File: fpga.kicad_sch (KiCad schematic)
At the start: 36 parts, among them U201 ICE40HX4K, U202 W25Q16JV, U203 IS61WV25616FBLL-10TLI

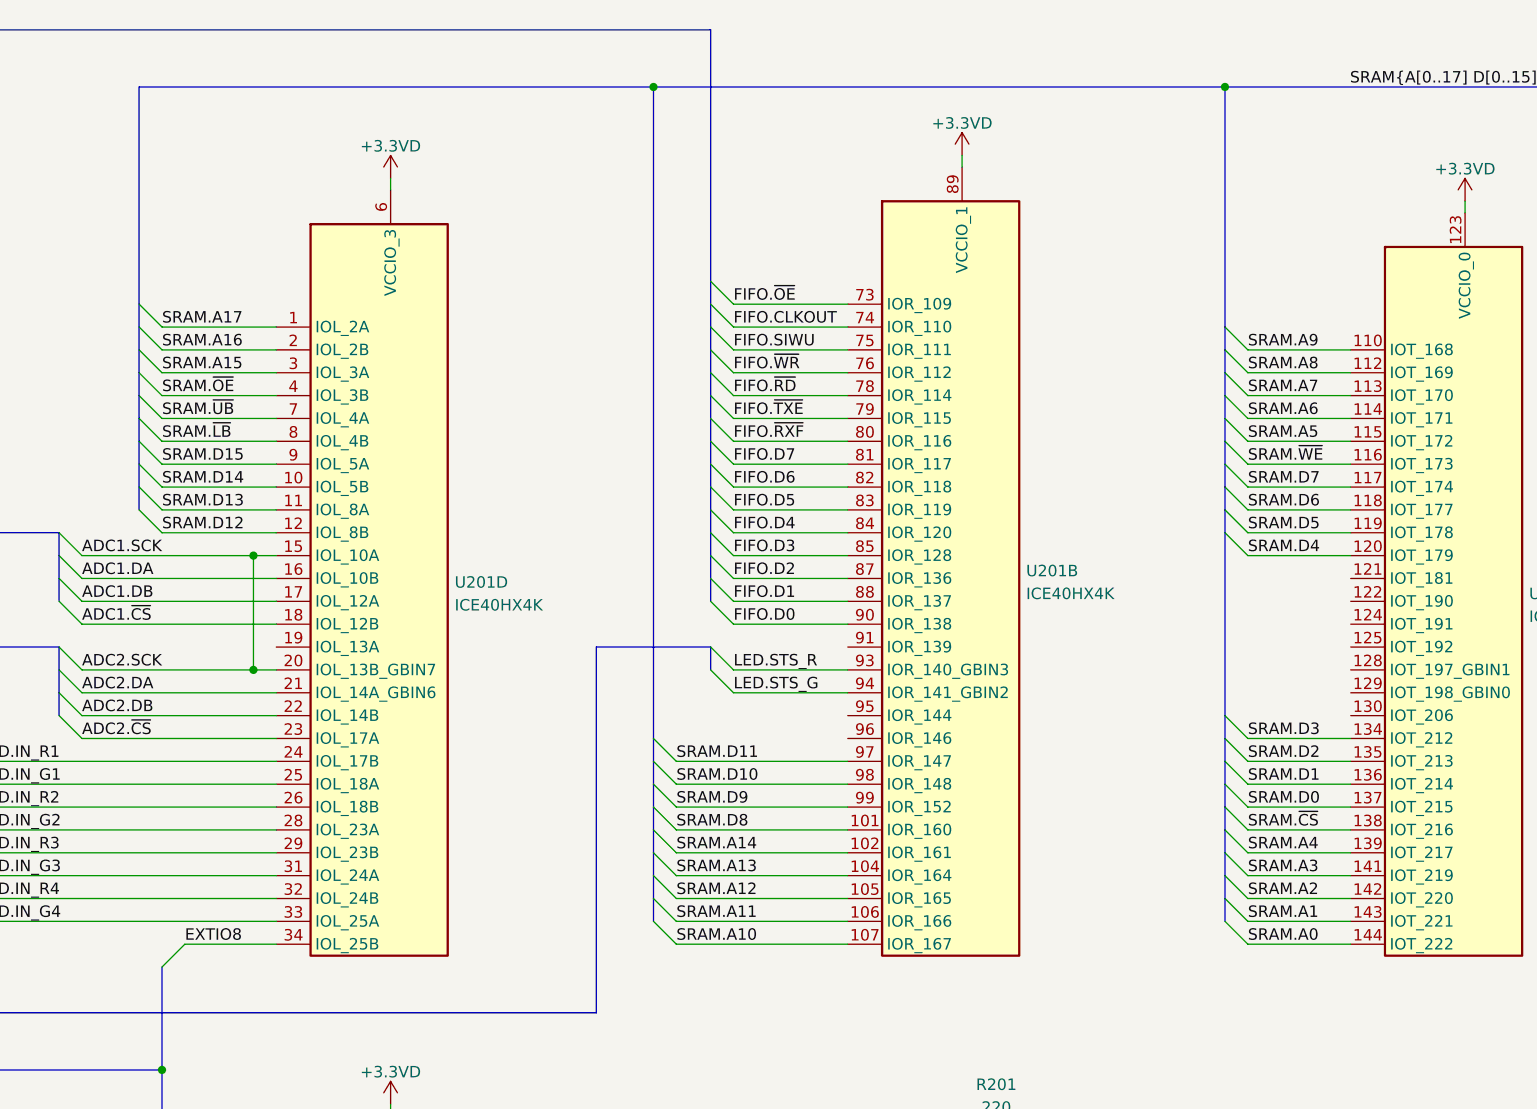
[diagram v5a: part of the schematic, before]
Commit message: Schematic: reconnect SRAM to ease PCB routing
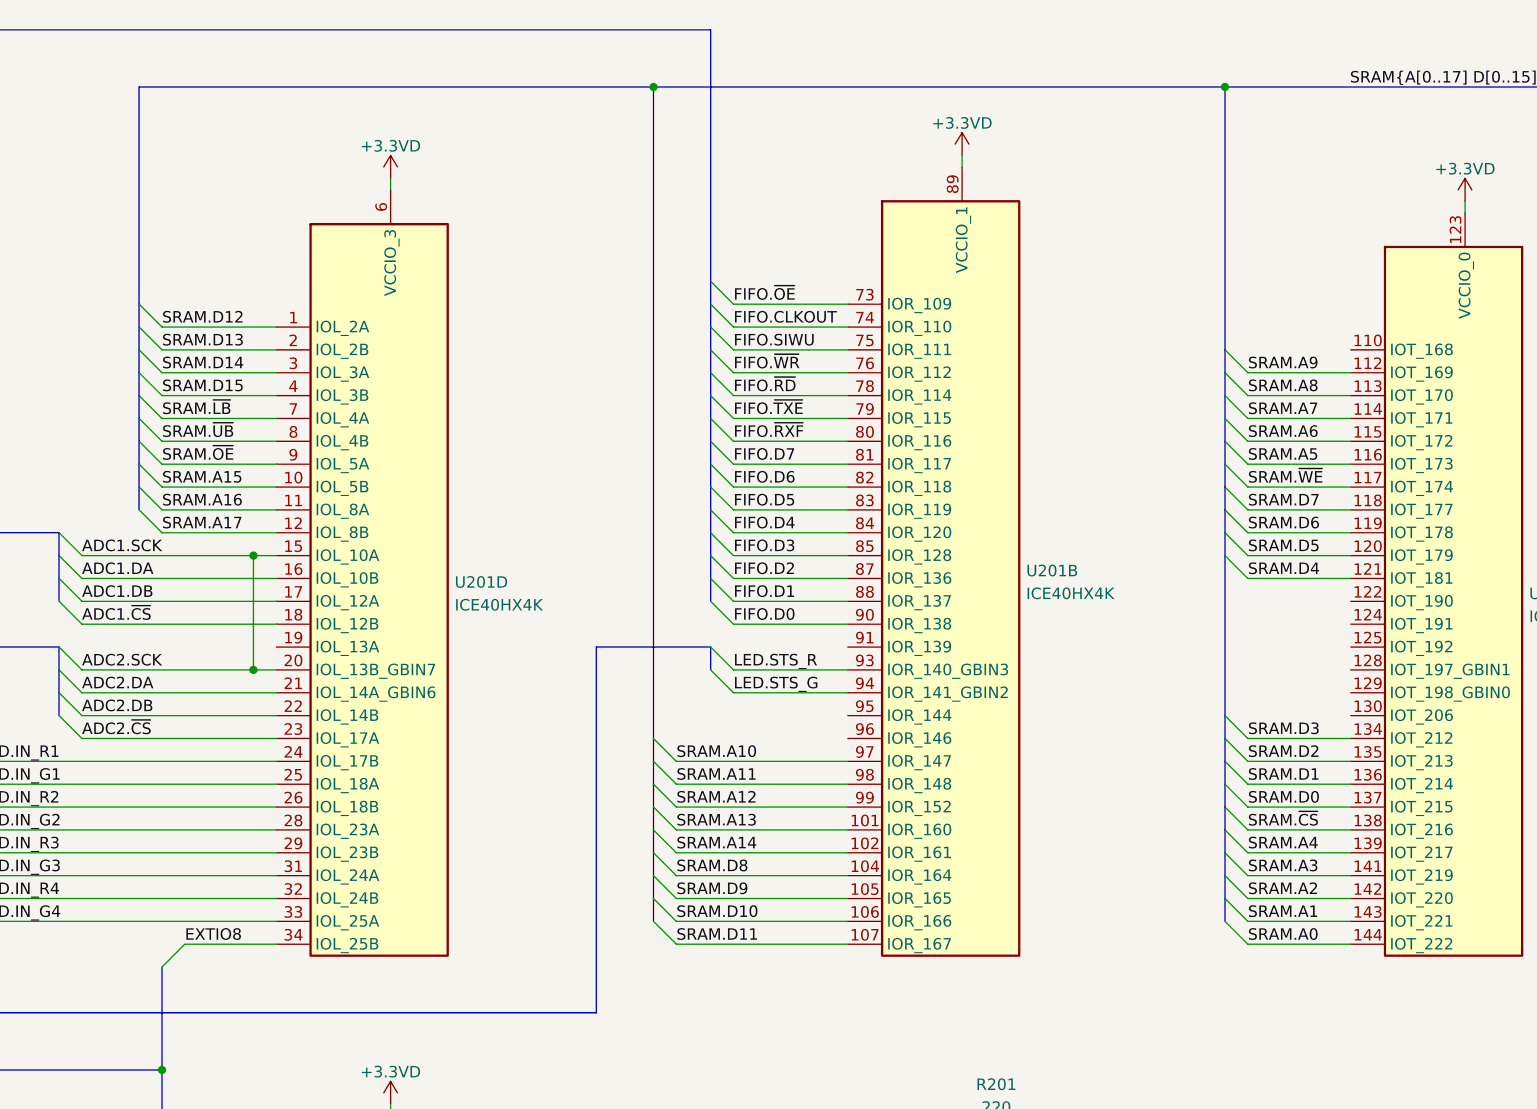
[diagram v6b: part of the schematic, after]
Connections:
- net SRAM.A10: now also U201.97 (IOR_147); no longer U201.107 (IOR_167)
- net SRAM.A11: now also U201.98 (IOR_148); no longer U201.106 (IOR_166)
- net SRAM.A12: now also U201.99 (IOR_152); no longer U201.105 (IOR_165)
- net SRAM.A13: now also U201.101 (IOR_160); no longer U201.104 (IOR_164)
- net SRAM.A15: now also U201.10 (IOL_5B); no longer U201.3 (IOL_3A)
- net SRAM.A16: now also U201.11 (IOL_8A); no longer U201.2 (IOL_2B)
- net SRAM.A17: now also U201.12 (IOL_8B); no longer U201.1 (IOL_2A)
- net SRAM.A5: now also U201.116 (IOT_173); no longer U201.115 (IOT_172)
- net SRAM.A6: now also U201.115 (IOT_172); no longer U201.114 (IOT_171)
- net SRAM.A7: now also U201.114 (IOT_171); no longer U201.113 (IOT_170)
- net SRAM.A8: now also U201.113 (IOT_170); no longer U201.112 (IOT_169)
- net SRAM.A9: now also U201.112 (IOT_169); no longer U201.110 (IOT_168)
- net SRAM.D10: now also U201.106 (IOR_166); no longer U201.98 (IOR_148)
- net SRAM.D11: now also U201.107 (IOR_167); no longer U201.97 (IOR_147)
- net SRAM.D12: now also U201.1 (IOL_2A); no longer U201.12 (IOL_8B)
- net SRAM.D13: now also U201.2 (IOL_2B); no longer U201.11 (IOL_8A)
- net SRAM.D14: now also U201.3 (IOL_3A); no longer U201.10 (IOL_5B)
- net SRAM.D15: now also U201.4 (IOL_3B); no longer U201.9 (IOL_5A)
- net SRAM.D4: now also U201.121 (IOT_181); no longer U201.120 (IOT_179)
- net SRAM.D5: now also U201.120 (IOT_179); no longer U201.119 (IOT_178)
- net SRAM.D6: now also U201.119 (IOT_178); no longer U201.118 (IOT_177)
- net SRAM.D7: now also U201.118 (IOT_177); no longer U201.117 (IOT_174)
- net SRAM.D8: now also U201.104 (IOR_164); no longer U201.101 (IOR_160)
- net SRAM.D9: now also U201.105 (IOR_165); no longer U201.99 (IOR_152)
- net SRAM.~{LB}: now also U201.7 (IOL_4A); no longer U201.8 (IOL_4B)
- net SRAM.~{OE}: now also U201.9 (IOL_5A); no longer U201.4 (IOL_3B)
- net SRAM.~{UB}: now also U201.8 (IOL_4B); no longer U201.7 (IOL_4A)
- net SRAM.~{WE}: now also U201.117 (IOT_174); no longer U201.116 (IOT_173)

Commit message: FPGA: connect LEDs differently
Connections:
- net LED.IN_G1: now also U201.28 (IOL_23A); no longer U201.25 (IOL_18A)
- net LED.IN_G2: now also U201.26 (IOL_18B); no longer U201.28 (IOL_23A)
- net LED.IN_G3: now also U201.33 (IOL_25A); no longer U201.31 (IOL_24A)
- net LED.IN_G4: now also U201.32 (IOL_24B); no longer U201.33 (IOL_25A)
- net LED.IN_R2: now also U201.25 (IOL_18A); no longer U201.26 (IOL_18B)
- net LED.IN_R4: now also U201.31 (IOL_24A); no longer U201.32 (IOL_24B)
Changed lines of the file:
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@@
     (effects (font (size 1.27 1.27)) (justify left bottom))
   )
-  (label "LED.IN_R4" (at 115.57 120.65 0)
+  (label "LED.IN_R4" (at 115.57 118.11 0)
     (effects (font (size 1.27 1.27)) (justify left bottom))
   )
@@
     (effects (font (size 1.27 1.27)) (justify left bottom))
   )
-  (label "LED.IN_G3" (at 115.57 118.11 0)
+  (label "LED.IN_G3" (at 115.57 123.19 0)
     (effects (font (size 1.27 1.27)) (justify left bottom))
   )
@@
     (effects (font (size 1.27 1.27)) (justify left bottom))
   )
-  (label "LED.IN_G4" (at 115.57 123.19 0)
+  (label "LED.IN_G4" (at 115.57 120.65 0)
     (effects (font (size 1.27 1.27)) (justify left bottom))
   )
@@
     (effects (font (size 1.27 1.27)) (justify left bottom))
   )
-  (label "LED.IN_G1" (at 115.57 107.95 0)
+  (label "LED.IN_G1" (at 115.57 113.03 0)
     (effects (font (size 1.27 1.27)) (justify left bottom))
   )
@@
     (effects (font (size 1.27 1.27)) (justify left bottom))
   )
-  (label "LED.IN_R2" (at 115.57 110.49 0)
+  (label "LED.IN_R2" (at 115.57 107.95 0)
     (effects (font (size 1.27 1.27)) (justify left bottom))
   )
@@
     (effects (font (size 1.27 1.27)) (justify left bottom))
   )
-  (label "LED.IN_G2" (at 115.57 113.03 0)
-    (effects (font (size 1.27 1.27)) (justify left bottom))
-  )
+  (label "LED.IN_G2" (at 115.57 110.49 0)
+    (effects (font (size 1.27 1.27)) (justify left bottom))
+  )

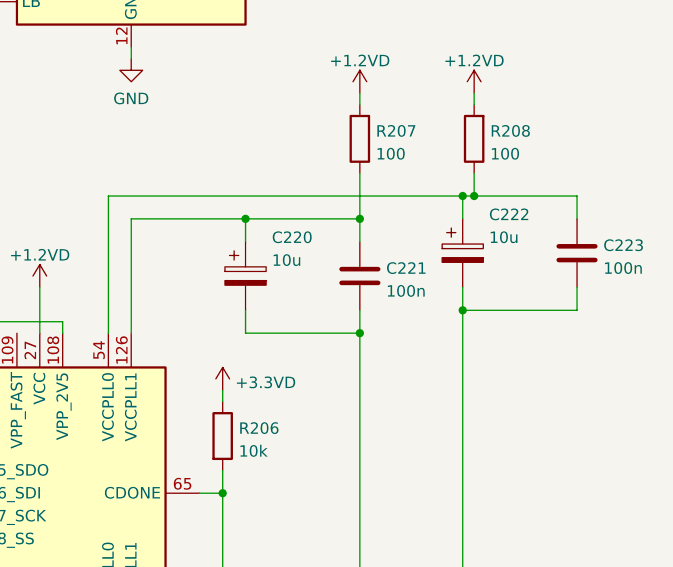
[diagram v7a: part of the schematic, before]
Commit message: Replace 10uf al-elco by tantalum -Space savings (0805 vs 4mm cylinder)
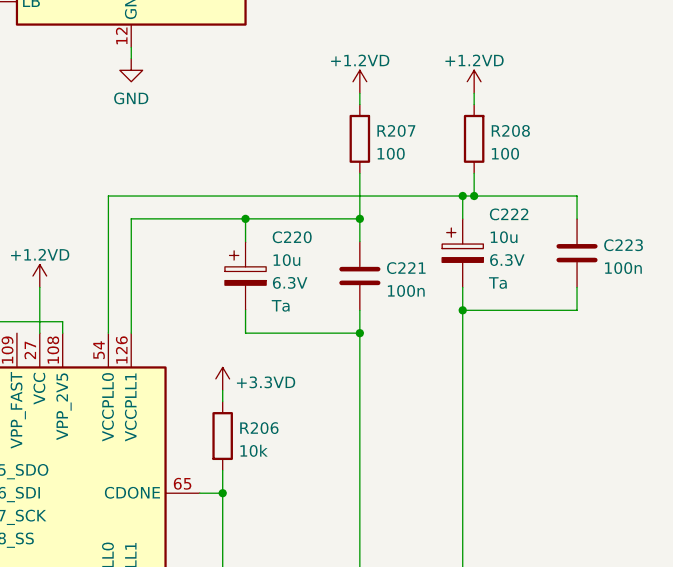
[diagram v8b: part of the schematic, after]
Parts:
- C220, C222: footprint Capacitor_SMD:CP_Elec_4x5.8 -> Capacitor_Tantalum_SMD:CP_EIA-2012-15_AVX-P; Mfr Nichicon -> AVX; Mfr PN UCL1C100MCL1GS -> TCJN106M006R0500; Spec1 (none) -> 6.3V; Spec2 (none) -> Ta
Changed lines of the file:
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@@
       (effects (font (size 1.27 1.27)) (justify left))
     )
-    (property "Footprint" "Capacitor_SMD:CP_Elec_4x5.8" (id 2) (at 380.6952 156.21 0)
+    (property "Footprint" "Capacitor_Tantalum_SMD:CP_EIA-2012-15_AVX-P" (id 2) (at 380.6952 156.21 0)
       (effects (font (size 1.27 1.27)) hide)
     )
@@
       (effects (font (size 1.27 1.27)) hide)
     )
-    (property "Spec1" "" (id 4) (at 382.651 153.2132 0)
+    (property "Spec1" "6.3V" (id 4) (at 382.651 153.2132 0)
       (effects (font (size 1.27 1.27)) (justify left))
     )
-    (property "Spec2" "" (id 5) (at 382.651 155.7501 0)
+    (property "Spec2" "Ta" (id 5) (at 382.651 155.7501 0)
       (effects (font (size 1.27 1.27)) (justify left))
     )
-    (property "Tolerance" "" (id 6) (at 379.73 152.4 0)
+    (property "Mfr" "AVX" (id 7) (at 379.73 152.4 0)
       (effects (font (size 1.27 1.27)) hide)
     )
-    (property "Mfr" "Nichicon" (id 7) (at 379.73 152.4 0)
-      (effects (font (size 1.27 1.27)) hide)
-    )
-    (property "Mfr PN" "UCL1C100MCL1GS" (id 8) (at 379.73 152.4 0)
+    (property "Mfr PN" "TCJN106M006R0500" (id 8) (at 379.73 152.4 0)
       (effects (font (size 1.27 1.27)) hide)
     )
@@
       (effects (font (size 1.27 1.27)) (justify left))
     )
-    (property "Footprint" "Capacitor_SMD:CP_Elec_4x5.8" (id 2) (at 356.5652 158.75 0)
+    (property "Footprint" "Capacitor_Tantalum_SMD:CP_EIA-2012-15_AVX-P" (id 2) (at 356.5652 158.75 0)
       (effects (font (size 1.27 1.27)) hide)
     )
@@
       (effects (font (size 1.27 1.27)) hide)
     )
-    (property "Spec1" "" (id 4) (at 358.521 155.7532 0)
+    (property "Spec1" "6.3V" (id 4) (at 358.521 155.7532 0)
       (effects (font (size 1.27 1.27)) (justify left))
     )
-    (property "Spec2" "" (id 5) (at 358.521 158.2901 0)
+    (property "Spec2" "Ta" (id 5) (at 358.521 158.2901 0)
       (effects (font (size 1.27 1.27)) (justify left))
     )
-    (property "Tolerance" "" (id 6) (at 355.6 154.94 0)
+    (property "Mfr" "AVX" (id 7) (at 355.6 154.94 0)
       (effects (font (size 1.27 1.27)) hide)
     )
-    (property "Mfr" "Nichicon" (id 7) (at 355.6 154.94 0)
+    (property "Mfr PN" "TCJN106M006R0500" (id 8) (at 355.6 154.94 0)
       (effects (font (size 1.27 1.27)) hide)
     )
-    (property "Mfr PN" "UCL1C100MCL1GS" (id 8) (at 355.6 154.94 0)
-      (effects (font (size 1.27 1.27)) hide)
-    )
